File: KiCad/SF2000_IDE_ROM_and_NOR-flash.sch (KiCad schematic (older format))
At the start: 7 parts, among them J5 IDE_ATA_44pin, U13 SST39LF040, U14 SST39LF802C, U15 74LVC245A, U16 74LVC245A, U17 74LVC245A

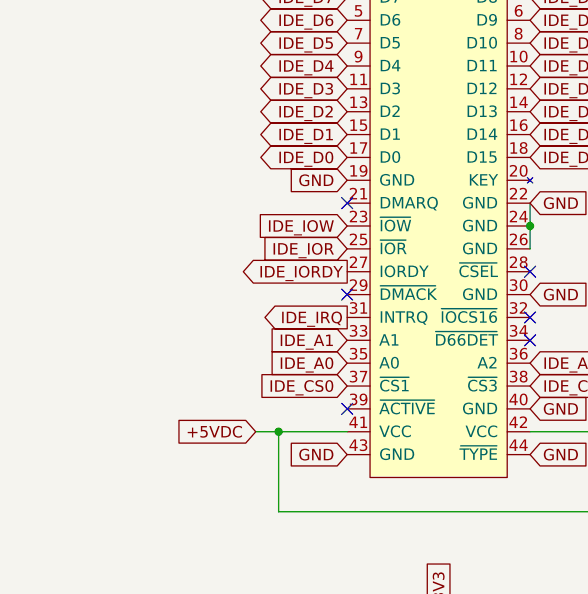
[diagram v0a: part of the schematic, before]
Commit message: added R5,R6 pull-up/down resistors on IDE, added +5V-header for external powering during standalone programming FPGA
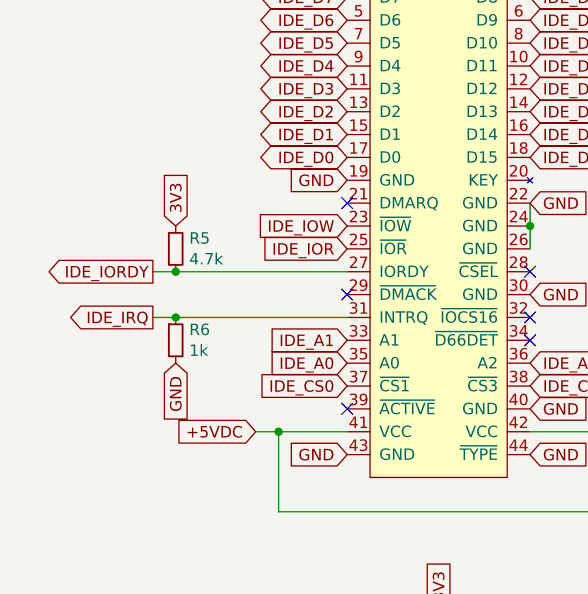
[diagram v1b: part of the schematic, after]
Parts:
- added R5: 4.7k, Resistor_SMD:R_0805_2012Metric_Pad1.15x1.40mm_HandSolder, symbol Device:R_Small
- added R6: 1k, Resistor_SMD:R_0805_2012Metric_Pad1.15x1.40mm_HandSolder, symbol Device:R_Small
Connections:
- net 3V3: now also R5.1
- net GND: now also R6.2
- net IDE_IORDY: now also R5.2
- net IDE_IRQ: now also R6.1
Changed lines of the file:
@@
 NoConn ~ 3100 3050
 NoConn ~ 2300 2750
-Text GLabel 2300 3050 0    50   Output ~ 0
+Text GLabel 1450 3050 0    50   Output ~ 0
 IDE_IORDY
 NoConn ~ 2300 3150
-Text GLabel 2300 3250 0    50   Output ~ 0
+Text GLabel 1450 3250 0    50   Output ~ 0
 IDE_IRQ
 Text GLabel 2200 5150 0    50   Input ~ 0
@@
 Text GLabel 6100 1500 1    50   Input ~ 0
 3V3
+$Comp
+L Device:R_Small R?
+U 1 1 62340B55
+P 1550 2950
+AR Path="/62340B55" Ref="R?"  Part="1"
+AR Path="/620D263D/62340B55" Ref="R?"  Part="1"
+AR Path="/627A6500/62340B55" Ref="R5"  Part="1"
+F 0 "R5" H 1609 2996 50  0000 L CNN
+F 1 "4.7k" H 1609 2905 50  0000 L CNN
+F 2 "Resistor_SMD:R_0805_2012Metric_Pad1.15x1.40mm_HandSolder" H 1550 2950 50  0001 C CNN
+F 3 "~" H 1550 2950 50  0001 C CNN
+	1    1550 2950
+	1    0    0    -1
+$EndComp
+$Comp
+L Device:R_Small R?
+U 1 1 62340D58
+P 1550 3350
+AR Path="/62340D58" Ref="R?"  Part="1"
+AR Path="/620D263D/62340D58" Ref="R?"  Part="1"
+AR Path="/627A6500/62340D58" Ref="R6"  Part="1"
+F 0 "R6" H 1609 3396 50  0000 L CNN
+F 1 "1k" H 1609 3305 50  0000 L CNN
+F 2 "Resistor_SMD:R_0805_2012Metric_Pad1.15x1.40mm_HandSolder" H 1550 3350 50  0001 C CNN
+F 3 "~" H 1550 3350 50  0001 C CNN
+	1    1550 3350
+	1    0    0    -1
+$EndComp
+Text GLabel 1550 3450 3    50   Input ~ 0
+GND
+Connection ~ 1550 3250
+Wire Wire Line
+	1550 3250 1450 3250
+Wire Wire Line
+	1550 3250 2300 3250
+Wire Wire Line
+	2300 3050 1550 3050
+Connection ~ 1550 3050
+Wire Wire Line
+	1550 3050 1450 3050
+Text GLabel 1550 2850 1    50   Input ~ 0
+3V3
 $EndSCHEMATC

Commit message: added IDE Activity LED-header and a header for IDE-pin 39 /Active
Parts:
- renumbered U13 to U14, U14 to U15, U15 to U16, U16 to U17, U17 to U18
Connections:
- net ACTIVE: now reaches J5.39 (~ACTIVE)
- no-connect marks 7 -> 6
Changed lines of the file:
@@
 $EndComp
 $Comp
-L SF2000:SST39LF040 U13
+L SF2000:SST39LF040 U14
 U 1 1 627D2ECC
 P 6100 2600
-F 0 "U13" H 6100 2600 50  0000 C CNN
+F 0 "U14" H 6100 2600 50  0000 C CNN
 F 1 "SST39LF040" V 6100 2200 50  0000 C CNN
 F 2 "SF2000:PLCC-32_11.4x14.0mm_P1.27mm" H 6100 2600 50  0001 C CNN
@@
 $EndComp
 $Comp
-L SF2000:SST39LF802C-55-4C-EKE U14
+L SF2000:SST39LF802C-55-4C-EKE U15
 U 1 1 627FF0EA
 P 9050 2700
-F 0 "U14" H 9050 4025 50  0000 C CNN
+F 0 "U15" H 9050 4025 50  0000 C CNN
 F 1 "SST39LF802C" H 9050 3934 50  0000 C CNN
 F 2 "Package_SO:TSOP-I-48_18.4x12mm_P0.5mm" H 9050 3250 50  0001 C CNN
@@
 Text GLabel 3100 3550 2    50   Input ~ 0
 IDE_CS1
-NoConn ~ 2300 3650
 Text GLabel 3100 3650 2    50   Input ~ 0
 GND
@@
 NoConn ~ 3100 3350
 $Comp
-L SF2000:74LVC245A U15
+L SF2000:74LVC245A U16
 U 1 1 628D607F
 P 2700 5350
-F 0 "U15" H 2700 5200 50  0000 C CNN
+F 0 "U16" H 2700 5200 50  0000 C CNN
 F 1 "74LVC245A" H 2350 6100 50  0000 C CNN
 F 2 "Package_SO:TSSOP-20_4.4x6.5mm_P0.65mm" H 2700 5350 50  0001 C CNN
@@
 IDE_CS0
 $Comp
-L SF2000:74LVC245A U17
+L SF2000:74LVC245A U18
 U 1 1 628E9EE2
 P 6550 5350
-F 0 "U17" H 6550 5200 50  0000 C CNN
+F 0 "U18" H 6550 5200 50  0000 C CNN
 F 1 "74LVC245A" H 6200 6100 50  0000 C CNN
 F 2 "Package_SO:TSSOP-20_4.4x6.5mm_P0.65mm" H 6550 5350 50  0001 C CNN
@@
 GND
 $Comp
-L SF2000:74LVC245A U16
+L SF2000:74LVC245A U17
 U 1 1 628ED6C8
 P 4650 5350
-F 0 "U16" H 4650 5200 50  0000 C CNN
+F 0 "U17" H 4650 5200 50  0000 C CNN
 F 1 "74LVC245A" H 4300 6100 50  0000 C CNN
 F 2 "Package_SO:TSSOP-20_4.4x6.5mm_P0.65mm" H 4650 5350 50  0001 C CNN
@@
 Text GLabel 1550 2850 1    50   Input ~ 0
 3V3
+Text GLabel 2300 3650 0    50   Input ~ 0
+ACTIVE
 $EndSCHEMATC

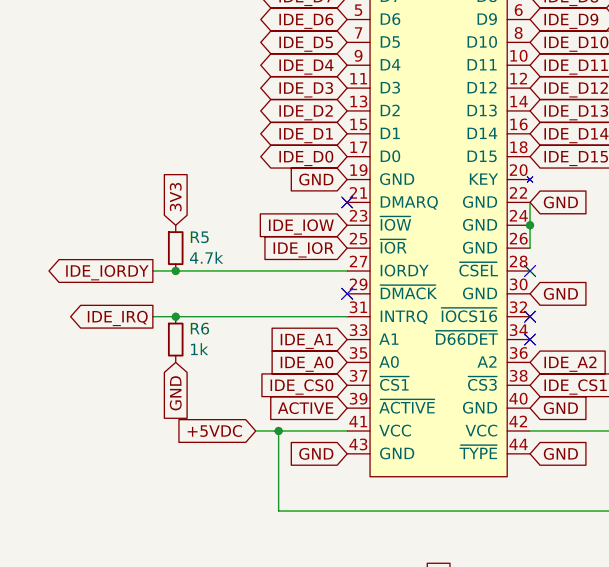
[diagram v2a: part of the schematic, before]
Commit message: fixed labeling/enumeration of caps and resistors, and some silkscreen fixes
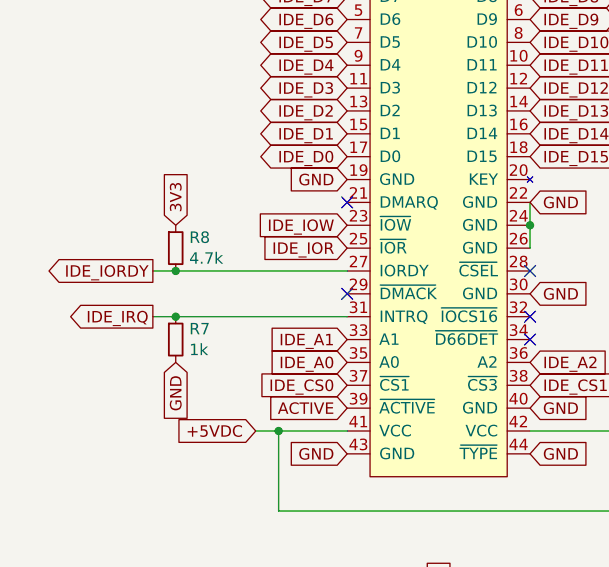
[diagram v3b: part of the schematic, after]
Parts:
- renumbered R6 to R7, R5 to R8
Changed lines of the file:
@@
 AR Path="/62340B55" Ref="R?"  Part="1"
 AR Path="/620D263D/62340B55" Ref="R?"  Part="1"
-AR Path="/627A6500/62340B55" Ref="R5"  Part="1"
-F 0 "R5" H 1609 2996 50  0000 L CNN
+AR Path="/627A6500/62340B55" Ref="R8"  Part="1"
+F 0 "R8" H 1609 2996 50  0000 L CNN
 F 1 "4.7k" H 1609 2905 50  0000 L CNN
 F 2 "Resistor_SMD:R_0805_2012Metric_Pad1.15x1.40mm_HandSolder" H 1550 2950 50  0001 C CNN
@@
 AR Path="/62340D58" Ref="R?"  Part="1"
 AR Path="/620D263D/62340D58" Ref="R?"  Part="1"
-AR Path="/627A6500/62340D58" Ref="R6"  Part="1"
-F 0 "R6" H 1609 3396 50  0000 L CNN
+AR Path="/627A6500/62340D58" Ref="R7"  Part="1"
+F 0 "R7" H 1609 3396 50  0000 L CNN
 F 1 "1k" H 1609 3305 50  0000 L CNN
 F 2 "Resistor_SMD:R_0805_2012Metric_Pad1.15x1.40mm_HandSolder" H 1550 3350 50  0001 C CNN

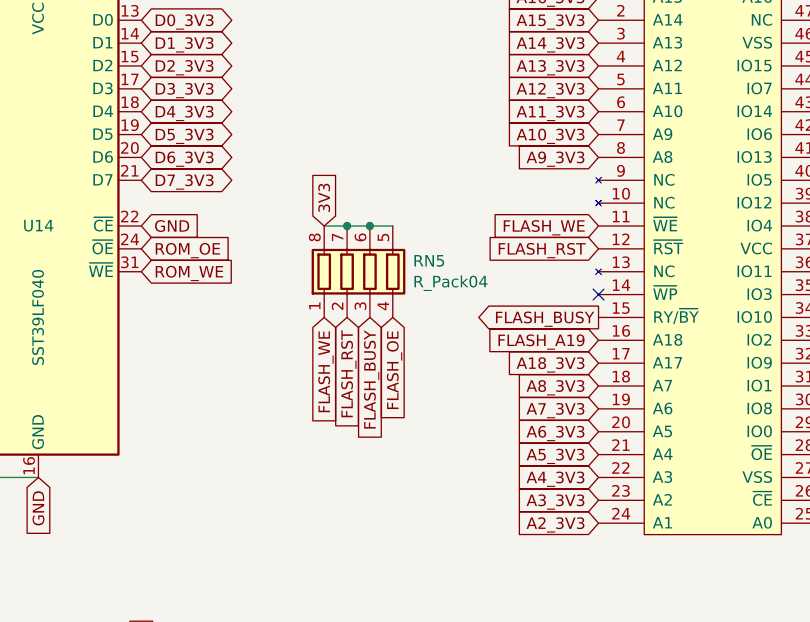
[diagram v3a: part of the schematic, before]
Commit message: Removed RN5 and R10 (ROM_WE) pull-up resistors, using FPGA's built-in pull-ups instead.
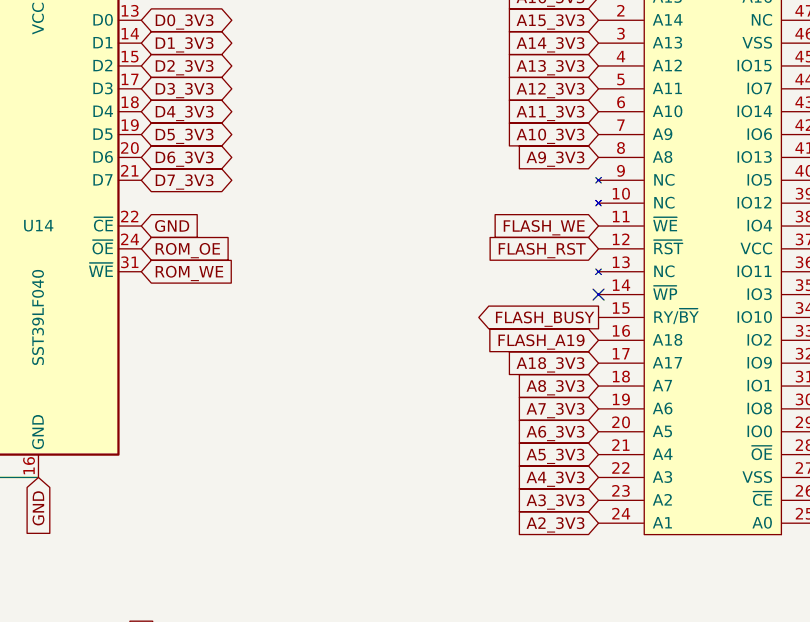
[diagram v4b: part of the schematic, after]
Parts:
- removed RN5: R_Pack04, SF2000:RESCAF80P320X160X60-8N, symbol Device:R_Pack04
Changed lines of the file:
@@
 	5650 3500 5650 3400
 NoConn ~ 8550 2900
-$Comp
-L Device:R_Pack04 RN?
-U 1 1 6206820D
-P 7550 2800
-AR Path="/620D263D/6206820D" Ref="RN?"  Part="1"
-AR Path="/627A6500/6206820D" Ref="RN5"  Part="1"
-F 0 "RN5" H 7738 2846 50  0000 L CNN
-F 1 "R_Pack04" H 7738 2755 50  0000 L CNN
-F 2 "SF2000:RESCAF80P320X160X60-8N" V 7825 2800 50  0001 C CNN
-F 3 "~" H 7550 2800 50  0001 C CNN
-	1    7550 2800
-	1    0    0    -1
-$EndComp
-Text GLabel 7350 2600 1    50   Input ~ 0
-3V3
-Wire Wire Line
-	7350 2600 7450 2600
-Connection ~ 7450 2600
-Wire Wire Line
-	7450 2600 7550 2600
-Connection ~ 7550 2600
-Wire Wire Line
-	7550 2600 7650 2600
-Text GLabel 7350 3000 3    50   Input ~ 0
-FLASH_WE
-Text GLabel 7450 3000 3    50   Input ~ 0
-FLASH_RST
-Text GLabel 7550 3000 3    50   Input ~ 0
-FLASH_BUSY
-Text GLabel 7650 3000 3    50   Input ~ 0
-FLASH_OE
 Text GLabel 6550 2800 2    50   Input ~ 0
 ROM_WE

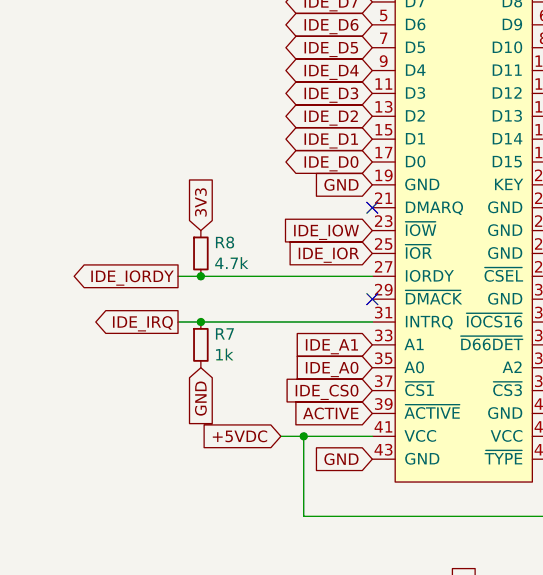
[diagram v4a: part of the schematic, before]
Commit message: removed CDAC-signal (not needed) and assigned E-signal to pin 11 (GCLKT_7) instead
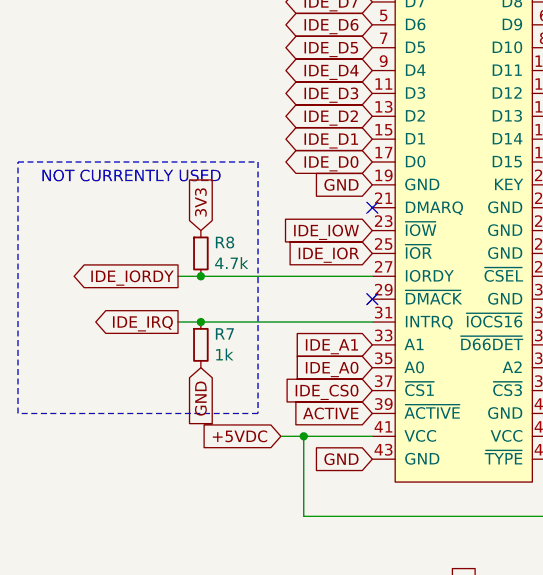
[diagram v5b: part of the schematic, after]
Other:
- note added: "NOT CURRENTLY USED"
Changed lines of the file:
@@
 Text GLabel 2300 3650 0    50   Input ~ 0
 ACTIVE
+Wire Notes Line
+	750  2550 1800 2550
+Wire Notes Line
+	1800 2550 1800 3650
+Wire Notes Line
+	1800 3650 750  3650
+Wire Notes Line
+	750  3650 750  2550
+Text Notes 850  2650 0    50   ~ 0
+NOT CURRENTLY USED
 $EndSCHEMATC

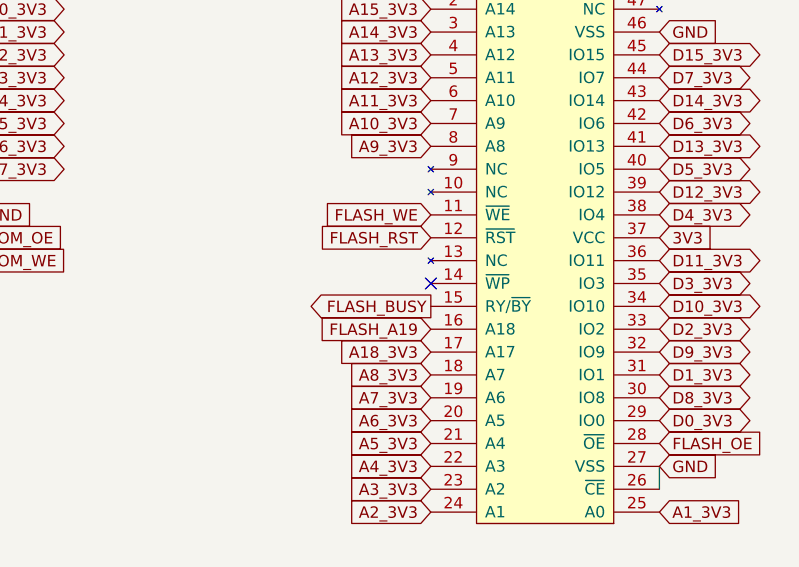
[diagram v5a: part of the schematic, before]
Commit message: Added resistor pack RN5 10k pull-ups for /WP, /AVEC, DONE, MODE
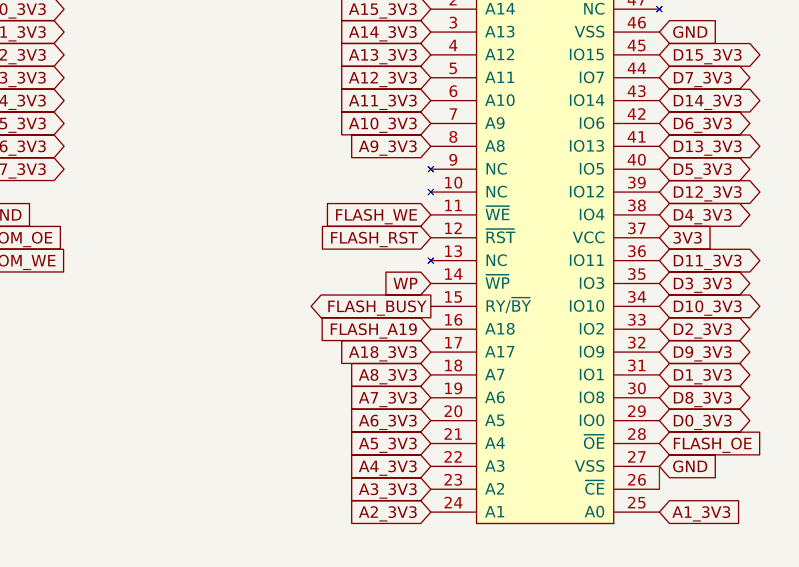
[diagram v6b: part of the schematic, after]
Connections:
- net WP: now reaches U15.14 (~WP)
- no-connect marks 6 -> 5
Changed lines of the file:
@@
 Wire Wire Line
 	5650 3500 5650 3400
-NoConn ~ 8550 2900
 Text GLabel 6550 2800 2    50   Input ~ 0
 ROM_WE
@@
 Text Notes 850  2650 0    50   ~ 0
 NOT CURRENTLY USED
+Text GLabel 8550 2900 0    50   Input ~ 0
+WP
 $EndSCHEMATC

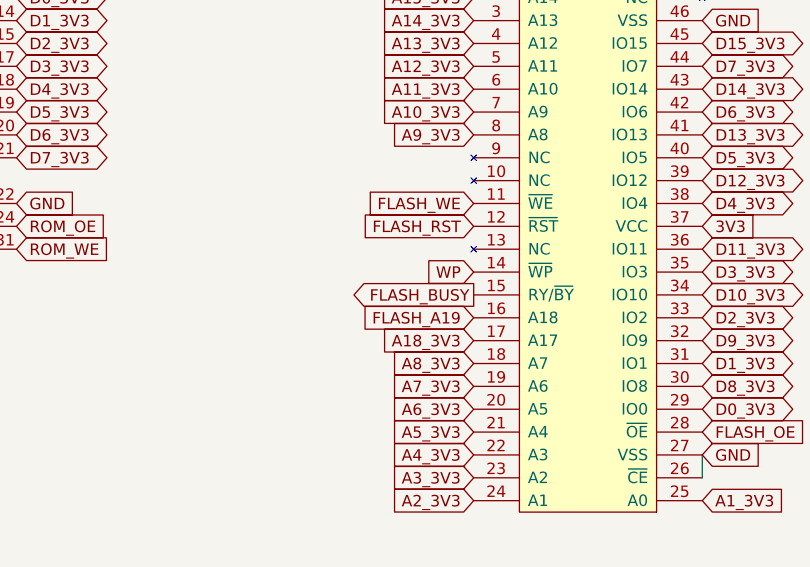
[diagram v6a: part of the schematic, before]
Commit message: Removed WP# and FLASH_BUSY signals
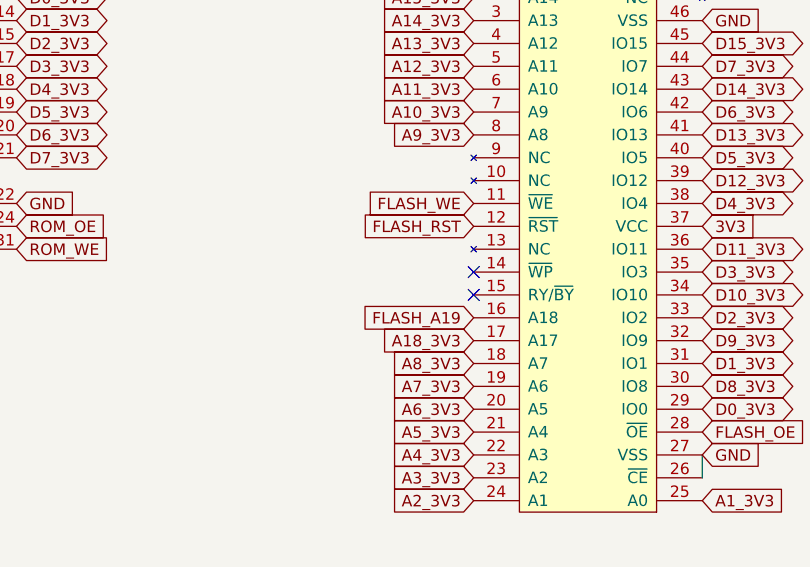
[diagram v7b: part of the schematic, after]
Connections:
- net FLASH_BUSY: no longer names the net of U15.15 (RY/~BY)
- net WP: no longer names the net of U15.14 (~WP)
- no-connect marks 5 -> 7
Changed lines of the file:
@@
 Text GLabel 8550 2700 0    50   Input ~ 0
 FLASH_RST
-Text GLabel 8550 3000 0    50   Output ~ 0
-FLASH_BUSY
 Text GLabel 6550 2700 2    50   Input ~ 0
 ROM_OE
@@
 Text Notes 850  2650 0    50   ~ 0
 NOT CURRENTLY USED
-Text GLabel 8550 2900 0    50   Input ~ 0
-WP
+NoConn ~ 8550 3000
+NoConn ~ 8550 2900
 $EndSCHEMATC

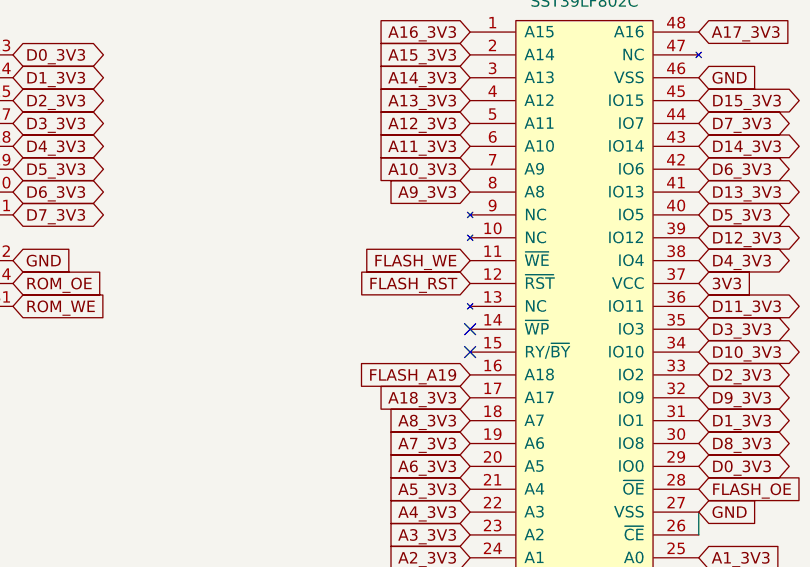
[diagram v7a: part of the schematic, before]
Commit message: Connect RST_3V3 to flash chip at U15
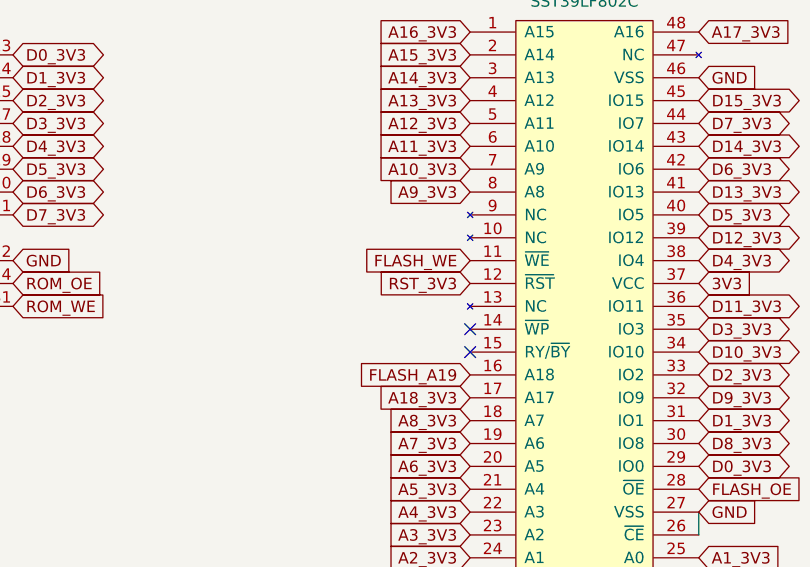
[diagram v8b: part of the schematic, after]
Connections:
- net FLASH_RST is gone; now on net RST_3V3: U15.12 (~RST)
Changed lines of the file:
@@
 Text GLabel 8550 2600 0    50   Input ~ 0
 FLASH_WE
-Text GLabel 8550 2700 0    50   Input ~ 0
-FLASH_RST
 Text GLabel 6550 2700 2    50   Input ~ 0
 ROM_OE
@@
 NoConn ~ 8550 3000
 NoConn ~ 8550 2900
+Text GLabel 8550 2700 0    50   Input ~ 0
+RST_3V3
 $EndSCHEMATC
